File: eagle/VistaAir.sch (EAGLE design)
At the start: 12 parts

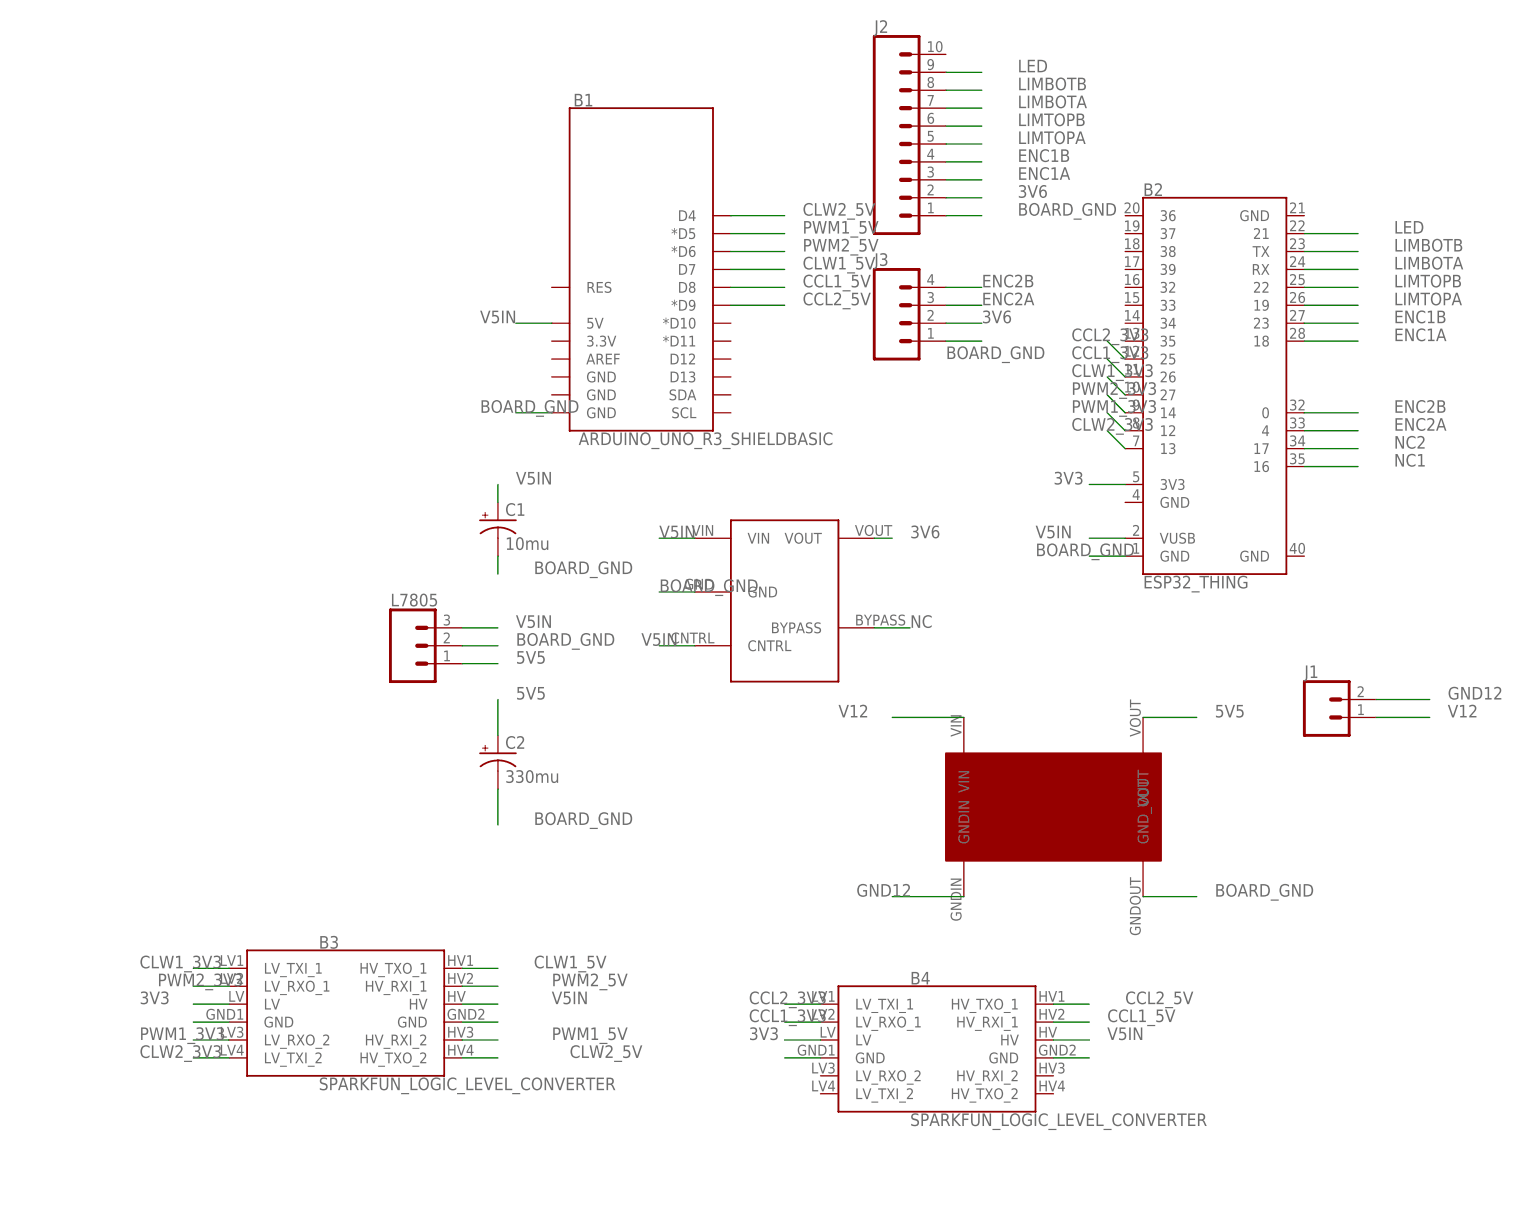
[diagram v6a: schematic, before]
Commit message: board tidy up, encoders working with modified library
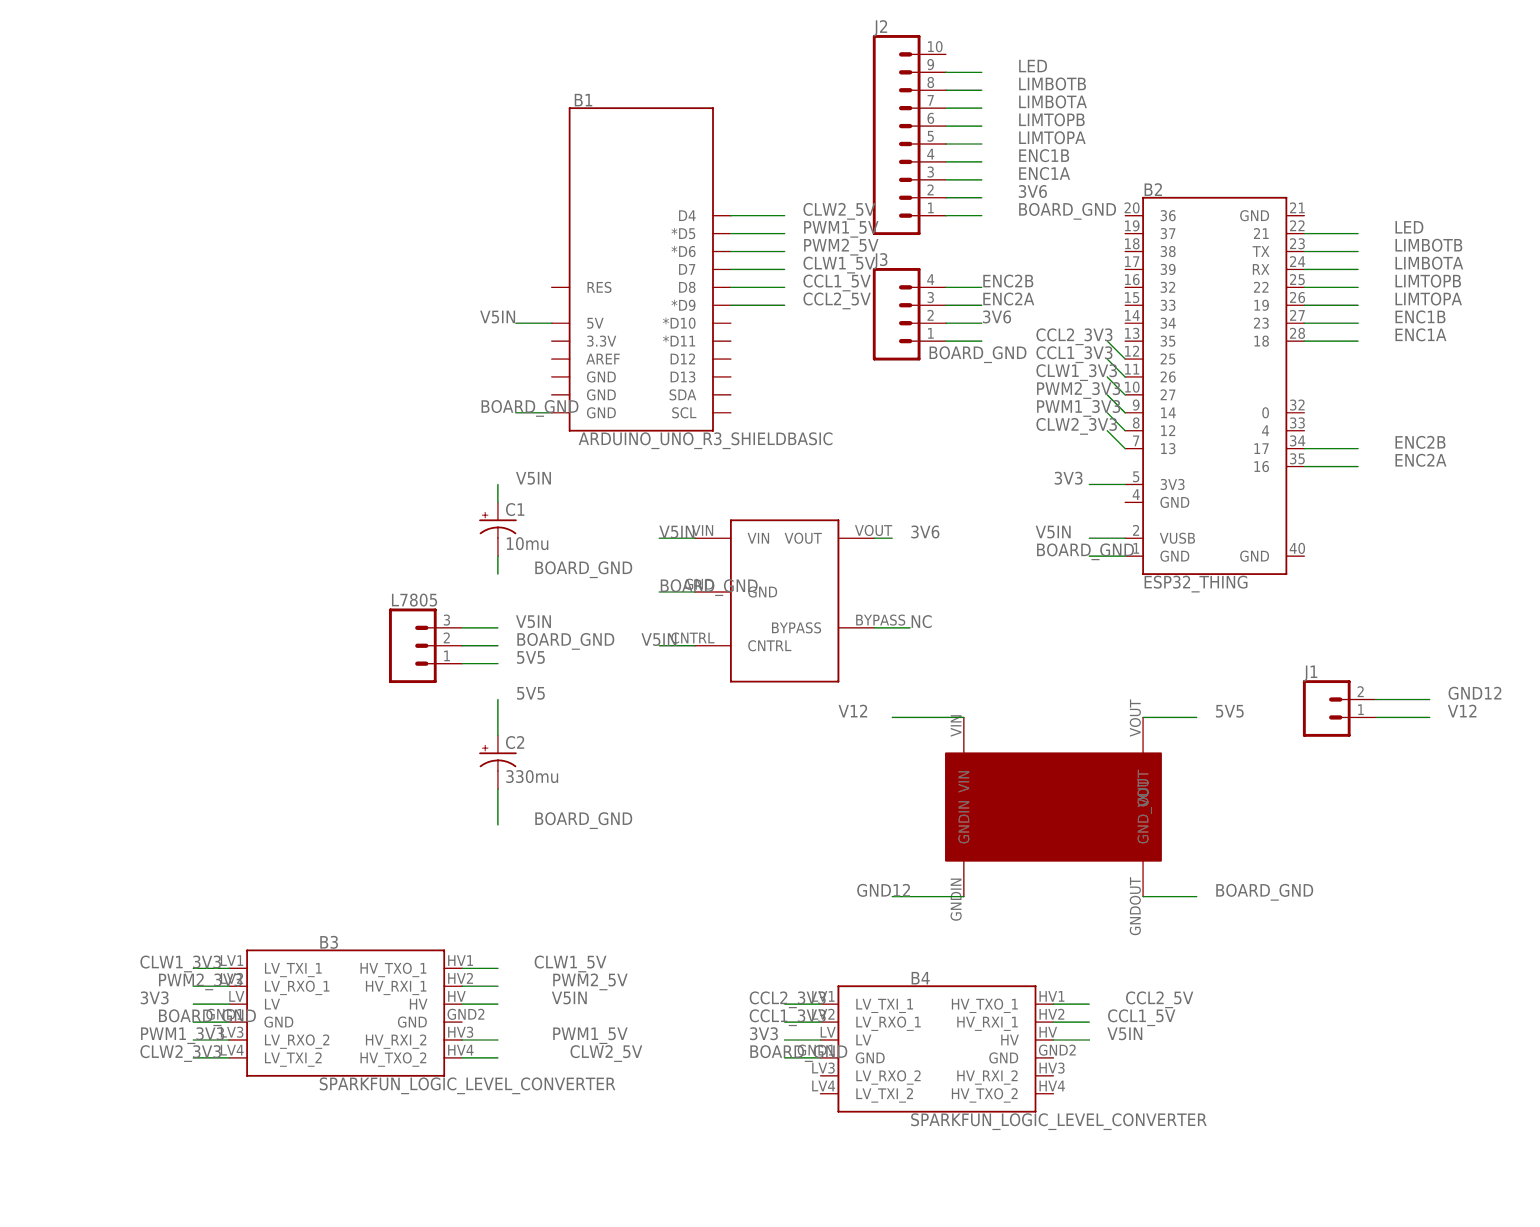
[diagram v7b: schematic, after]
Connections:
- removed net N$1: B3.GND
- removed net N$2: B3.GND@2
- removed net N$3: B4.GND
- removed net N$4: B4.GND@2
- removed net NC1: B2.16
- removed net NC2: B2.17
- net BOARD_GND: now also B3.GND, B4.GND
- net ENC2A: now also B2.16; no longer B2.4
- net ENC2B: now also B2.17; no longer B2.0
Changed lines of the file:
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@@
 <segment>
 <wire x1="114.3" y1="58.42" x2="111.76" y2="60.96" width="0.1524" layer="91"/>
-<label x="106.68" y="60.96" size="1.778" layer="95"/>
+<label x="101.6" y="60.96" size="1.778" layer="95"/>
 <pinref part="B2" gate="G$1" pin="27"/>
 </segment>
@@
 <segment>
 <wire x1="114.3" y1="55.88" x2="111.76" y2="58.42" width="0.1524" layer="91"/>
-<label x="106.68" y="58.42" size="1.778" layer="95"/>
+<label x="101.6" y="58.42" size="1.778" layer="95"/>
 <pinref part="B2" gate="G$1" pin="14"/>
 </segment>
@@
 <segment>
 <wire x1="114.3" y1="53.34" x2="111.76" y2="55.88" width="0.1524" layer="91"/>
-<label x="106.68" y="55.88" size="1.778" layer="95"/>
+<label x="101.6" y="55.88" size="1.778" layer="95"/>
 <pinref part="B2" gate="G$1" pin="12"/>
 </segment>
@@
 <segment>
 <wire x1="114.3" y1="50.8" x2="111.76" y2="53.34" width="0.1524" layer="91"/>
-<label x="106.68" y="53.34" size="1.778" layer="95"/>
+<label x="101.6" y="53.34" size="1.778" layer="95"/>
 <pinref part="B2" gate="G$1" pin="13"/>
 </segment>
@@
 <segment>
 <wire x1="114.3" y1="60.96" x2="111.76" y2="63.5" width="0.1524" layer="91"/>
-<label x="106.68" y="63.5" size="1.778" layer="95"/>
+<label x="101.6" y="63.5" size="1.778" layer="95"/>
 <pinref part="B2" gate="G$1" pin="26"/>
 </segment>
@@
 <segment>
 <wire x1="114.3" y1="63.5" x2="111.76" y2="66.04" width="0.1524" layer="91"/>
-<label x="106.68" y="66.04" size="1.778" layer="95"/>
+<label x="101.6" y="66.04" size="1.778" layer="95"/>
 <pinref part="B2" gate="G$1" pin="25"/>
 </segment>
@@
 <pinref part="J3" gate="G$1" pin="1"/>
 <wire x1="88.9" y1="66.04" x2="93.98" y2="66.04" width="0.1524" layer="91"/>
-<label x="88.9" y="63.5" size="1.778" layer="95"/>
+<label x="86.36" y="63.5" size="1.778" layer="95"/>
 </segment>
 <segment>
@@
 <label x="22.86" y="55.88" size="1.778" layer="95"/>
 </segment>
+<segment>
+<pinref part="B3" gate="G$1" pin="GND"/>
+<wire x1="-12.7" y1="-30.48" x2="-17.78" y2="-30.48" width="0.1524" layer="91"/>
+<label x="-22.86" y="-30.48" size="1.778" layer="95"/>
+</segment>
+<segment>
+<pinref part="B4" gate="G$1" pin="GND"/>
+<wire x1="71.12" y1="-35.56" x2="66.04" y2="-35.56" width="0.1524" layer="91"/>
+<label x="60.96" y="-35.56" size="1.778" layer="95"/>
+</segment>
 </net>
 <net name="ENC2B" class="0">
@@
 </segment>
 <segment>
-<wire x1="139.7" y1="55.88" x2="147.32" y2="55.88" width="0.1524" layer="91"/>
-<label x="152.4" y="55.88" size="1.778" layer="95"/>
-<pinref part="B2" gate="G$1" pin="0"/>
+<wire x1="139.7" y1="50.8" x2="147.32" y2="50.8" width="0.1524" layer="91"/>
+<label x="152.4" y="50.8" size="1.778" layer="95"/>
+<pinref part="B2" gate="G$1" pin="17"/>
 </segment>
 </net>
@@
 </segment>
 <segment>
-<wire x1="139.7" y1="53.34" x2="147.32" y2="53.34" width="0.1524" layer="91"/>
-<label x="152.4" y="53.34" size="1.778" layer="95"/>
-<pinref part="B2" gate="G$1" pin="4"/>
+<wire x1="139.7" y1="48.26" x2="147.32" y2="48.26" width="0.1524" layer="91"/>
+<label x="152.4" y="48.26" size="1.778" layer="95"/>
+<pinref part="B2" gate="G$1" pin="16"/>
 </segment>
 </net>
@@
 </segment>
 </net>
-<net name="NC1" class="0">
-<segment>
-<wire x1="139.7" y1="48.26" x2="147.32" y2="48.26" width="0.1524" layer="91"/>
-<label x="152.4" y="48.26" size="1.778" layer="95"/>
-<pinref part="B2" gate="G$1" pin="16"/>
-</segment>
-</net>
-<net name="NC2" class="0">
-<segment>
-<wire x1="139.7" y1="50.8" x2="147.32" y2="50.8" width="0.1524" layer="91"/>
-<label x="152.4" y="50.8" size="1.778" layer="95"/>
-<pinref part="B2" gate="G$1" pin="17"/>
-</segment>
-</net>
 <net name="5V5" class="1">
 <segment>
@@
 </segment>
 </net>
-<net name="N$1" class="0">
-<segment>
-<pinref part="B3" gate="G$1" pin="GND"/>
-<wire x1="-12.7" y1="-30.48" x2="-17.78" y2="-30.48" width="0.1524" layer="91"/>
-</segment>
-</net>
-<net name="N$2" class="0">
-<segment>
-<pinref part="B3" gate="G$1" pin="GND@2"/>
-<wire x1="20.32" y1="-30.48" x2="25.4" y2="-30.48" width="0.1524" layer="91"/>
-</segment>
-</net>
-<net name="N$3" class="0">
-<segment>
-<pinref part="B4" gate="G$1" pin="GND"/>
-<wire x1="71.12" y1="-35.56" x2="66.04" y2="-35.56" width="0.1524" layer="91"/>
-</segment>
-</net>
-<net name="N$4" class="0">
-<segment>
-<pinref part="B4" gate="G$1" pin="GND@2"/>
-<wire x1="104.14" y1="-35.56" x2="109.22" y2="-35.56" width="0.1524" layer="91"/>
-</segment>
-</net>
